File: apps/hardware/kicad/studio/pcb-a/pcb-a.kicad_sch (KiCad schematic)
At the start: 27 parts, among them J1 A PCB-K (JST-SH 10), J2 A portadora (IDC 2x15)

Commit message: feat(hardware): esquemático de la portadora de Studio y ajuste del apilado del panel
Portadora (rev 0.1, ERC sin violaciones):
- USB-C 5 V solo alimentación (CC 5.1 kΩ), polyfuse 3 A, TVS y bulk; VIN de la
  Teensy con el puente VUSB–VIN cortado.
- Teensy 4.1 como dos filas de 24 pines; USB host a USB-A; IDC 2×15 al panel con
  el mismo pinout de PCB-A; IDC 2×5 a los pines 1–10 de la Pi (5 V y UART).
- LEDs: pin 28 → 74AHCT1G125 a 5 V → puente de soldadura (saltar el buffer) → 330 Ω.
- Entrada estéreo: escalera 0/−10/−20 dB con palanca DP3T, acople, protección
  BAT54S sobre VREF de 1.65 V y seguidores MCP6004 hacia LINE IN del Audio Shield.
- Salidas 6.35 con acople, PHONES 3.5 con el sleeve en HP_VGND, CV OUT con RC de
  2 polos y seguidor.

Apilado del panel: PCB-A baja a −12.0 mm con separadores M3 estándar de 10 mm (buje
al ras, eje a 14.5 mm), PCB-K con agujeros de 8.0 mm y cuelga de los Choc, JST-SH de
entrada lateral entre placas. El pad estéreo no se lee (pin 25 libre).

Co-Authored-By: Claude Opus 5.5 <noreply@anthropic.com>
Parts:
- J1: footprint Connector_JST:JST_SH_BM10B-SRSS-TB_1x10-1MP_P1.00mm_Vertical -> Connector_JST:JST_SH_SM10B-SRSS-TB_1x10-1MP_P1.00mm_Horizontal
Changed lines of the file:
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@@
 		(date "2026-10-13")
 		(rev "0.1")
-		(comment 1 "5 ALPS EC11 (L=25, buje liso Ø6.8) + 2 RV09 B10K; placa a -11.5 mm bajo el aluminio")
+		(comment 1 "5 ALPS EC11 (L=25, buje liso Ø6.8) + 2 RV09 B10K; placa a -12.0 mm bajo el aluminio (separadores M3 de 10 mm)")
 		(comment 2 "Theory doc: apps/docs/variants/studio/theory/02-studio-pcb.md")
 	)
@@
 			)
 		)
-		(property "Footprint" "Connector_JST:JST_SH_BM10B-SRSS-TB_1x10-1MP_P1.00mm_Vertical"
+		(property "Footprint" "Connector_JST:JST_SH_SM10B-SRSS-TB_1x10-1MP_P1.00mm_Horizontal"
 			(at 229.87 149.86 0)
 			(hide yes)

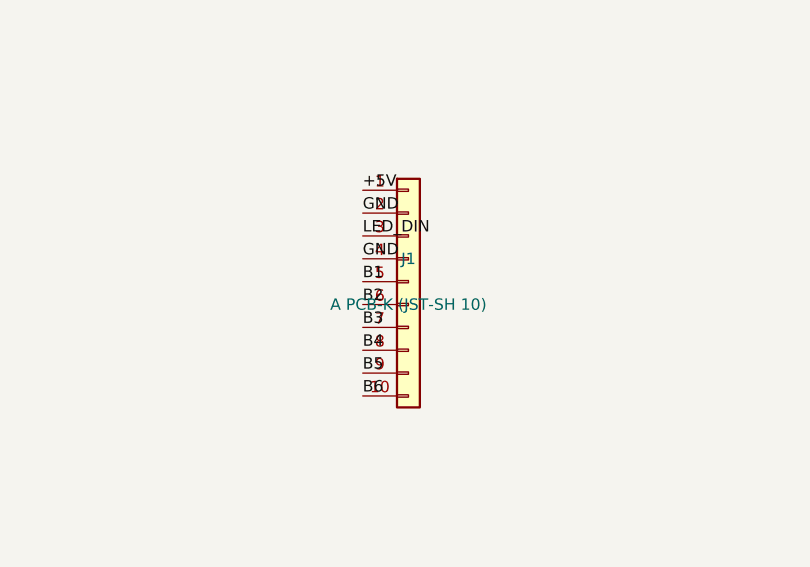
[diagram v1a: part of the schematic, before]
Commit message: feat(hardware): PCB-K ruteada (DRC limpio contra reglas de JLCPCB)
- Anillo de NAV: LEDs rotados 180° para que DOUT y DIN queden enfrentados en cada hueco (mismo
  orden e índices 0–11). Ruteo regular por script: anillo interior de +5V, saltos de datos por F.Cu
  que esquivan las ventanas de luz, una vía de GND por hueco (tools/route_pcb_k_ring.py).
- Zona de teclas con rutas explícitas (tools/route_pcb_k_keys.py): botones por F.Cu desde J1,
  cadena de datos y buses de +5V por B.Cu; capacitores de tecla a la derecha de cada LED; C19 sobre
  el bus de +5V; TP1/TP2 sobre sus pistas y fuera del BOM.
- Orden de pines de J1 nuevo en PCB-K y PCB-A (cable 1:1): B4, B6, B3, GND, +5V, GND, LED_DIN, B2,
  B5, B1. Evita ~14 cruces entre capas; los pines de la Teensy no cambian (02-studio-pcb.md §6.1).
- Planos de GND en F.Cu y B.Cu con costura cada 6 mm (tools/add_gnd_pours.py).
- Reglas de JLCPCB 2 capas en los tres proyectos: agujero-agujero 0.5 mm, vía ≥ 0.5/0.3, anillo
  ≥ 0.13; borde 0.25 mm (0.2 solo dentro de cada SK6812MINI-E).
- DRC con paridad de esquemático: 0 violaciones, 0 pads sin conectar, 0 errores de footprint.
- tools/route_board.py (Freerouting) queda como herramienta; no se usó en el resultado final.

Co-Authored-By: Claude Opus 5.5 <noreply@anthropic.com>
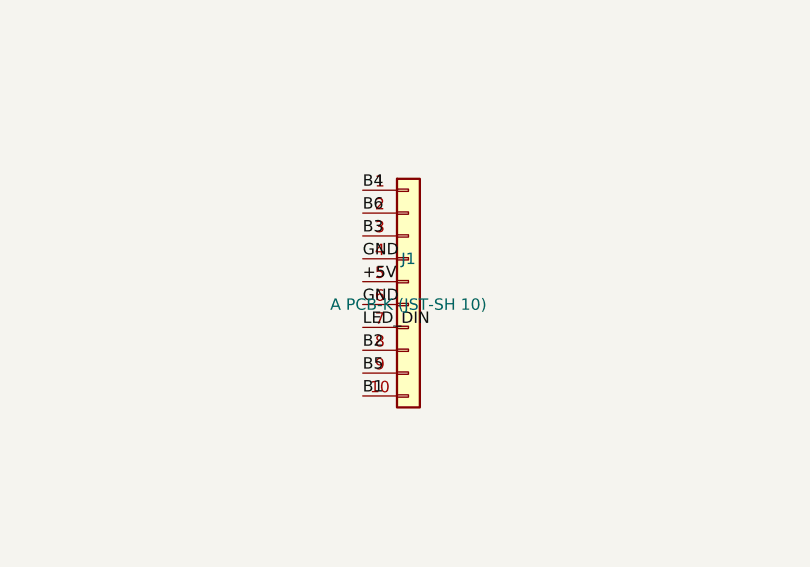
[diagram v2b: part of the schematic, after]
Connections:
- net +5V: now also J1.5 (Pin_5); no longer J1.1 (Pin_1)
- net B1: now also J1.10 (Pin_10); no longer J1.5 (Pin_5)
- net B2: now also J1.8 (Pin_8); no longer J1.6 (Pin_6)
- net B3: now also J1.3 (Pin_3); no longer J1.7 (Pin_7)
- net B4: now also J1.1 (Pin_1); no longer J1.8 (Pin_8)
- net B6: now also J1.2 (Pin_2); no longer J1.10 (Pin_10)
- net GND: now also J1.6 (Pin_6); no longer J1.2 (Pin_2)
- net LED_DIN: now also J1.7 (Pin_7); no longer J1.3 (Pin_3)
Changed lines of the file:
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@@
-	)
-	(label "+5V"
-		(at 224.79 139.70000000000002 0)
-		(effects
-			(font
-				(size 1.27 1.27)
-			)
-			(justify left bottom)
-		)
-	)
-	(label "GND"
-		(at 224.79 142.24 0)
-		(effects
-			(font
-				(size 1.27 1.27)
-			)
-			(justify left bottom)
-		)
-	)
-	(label "LED_DIN"
-		(at 224.79 144.78 0)
-		(effects
-			(font
-				(size 1.27 1.27)
-			)
-			(justify left bottom)
-		)
-	)
-	(label "GND"
-		(at 224.79 147.32000000000002 0)
-		(effects
-			(font
-				(size 1.27 1.27)
-			)
-			(justify left bottom)
-		)
-	)
-	(label "B1"
-		(at 224.79 149.86 0)
-		(effects
-			(font
-				(size 1.27 1.27)
-			)
-			(justify left bottom)
-		)
-	)
-	(label "B2"
-		(at 224.79 152.4 0)
-		(effects
-			(font
-				(size 1.27 1.27)
-			)
-			(justify left bottom)
-		)
-	)
-	(label "B3"
-		(at 224.79 154.94000000000003 0)
-		(effects
-			(font
-				(size 1.27 1.27)
-			)
-			(justify left bottom)
-		)
-	)
-	(label "B4"
-		(at 224.79 157.48000000000002 0)
-		(effects
-			(font
-				(size 1.27 1.27)
-			)
-			(justify left bottom)
-		)
-	)
-	(label "B5"
-		(at 224.79 160.02 0)
-		(effects
-			(font
-				(size 1.27 1.27)
-			)
-			(justify left bottom)
-		)
-	)
-	(label "B6"
-		(at 224.79 162.56 0)
-		(effects
-			(font
-				(size 1.27 1.27)
-			)
-			(justify left bottom)
-		)
 	)
 	(label "+5V"
@@
 			)
 			(justify left bottom)
+		)
+	)
+	(label "B4"
+		(at 224.79 139.70000000000002 0)
+		(effects
+			(font
+				(size 1.27 1.27)
+			)
+			(justify left bottom)
+		)
+	)
+	(label "B6"
+		(at 224.79 142.24 0)
+		(effects
+			(font
+				(size 1.27 1.27)
+			)
+			(justify left bottom)
+		)
+	)
+	(label "B3"
+		(at 224.79 144.78 0)
+		(effects
+			(font
+				(size 1.27 1.27)
+			)
+			(justify left bottom)
+		)
+	)
+	(label "GND"
+		(at 224.79 147.32000000000002 0)
+		(effects
+			(font
+				(size 1.27 1.27)
+			)
+			(justify left bottom)
+		)
+	)
+	(label "+5V"
+		(at 224.79 149.86 0)
+		(effects
+			(font
+				(size 1.27 1.27)
+			)
+			(justify left bottom)
+		)
+	)
+	(label "GND"
+		(at 224.79 152.4 0)
+		(effects
+			(font
+				(size 1.27 1.27)
+			)
+			(justify left bottom)
+		)
+	)
+	(label "LED_DIN"
+		(at 224.79 154.94000000000003 0)
+		(effects
+			(font
+				(size 1.27 1.27)
+			)
+			(justify left bottom)
+		)
+	)
+	(label "B2"
+		(at 224.79 157.48000000000002 0)
+		(effects
+			(font
+				(size 1.27 1.27)
+			)
+			(justify left bottom)
+		)
+	)
+	(label "B5"
+		(at 224.79 160.02 0)
+		(effects
+			(font
+				(size 1.27 1.27)
+			)
+			(justify left bottom)
+		)
+	)
+	(label "B1"
+		(at 224.79 162.56 0)
+		(effects
+			(font
+				(size 1.27 1.27)
+			)
+			(justify left bottom)

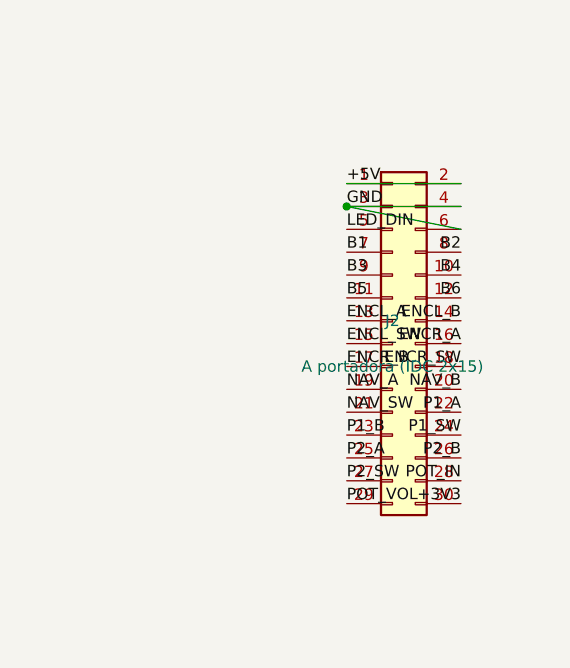
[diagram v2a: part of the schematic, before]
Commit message: feat(hardware): portadora ruteada (DRC limpio) y pinout del IDC reordenado
- Portadora: ruteo completo, DRC con paridad de esquemático 0/0/0 contra reglas de JLCPCB.
  +5V de F1 a la Pi en ~40 mm con una vía; sin paralelos audio↔digital a <1 mm.
- IDC 2×15 (PCB-A J2 ↔ portadora J5): pines ordenados por la X del pin de la Teensy al que van,
  para que el bus salga del conector sin cruces. Ambos esquemáticos re-etiquetados (ERC limpio),
  PCB-A re-ruteada (DRC 0/0/0). Tablas y razón en theory/02 §6.2.
- Herramientas: grid_route (Dijkstra en grilla 0.1 mm, 2 capas), finish_routing (rip-up and
  reroute de lo que deja Freerouting), clean_vias, add_gnd_escapes, fix_portadora_gnd,
  set_idc_pinout y build_portadora.sh (pipeline completo reproducible).

Co-Authored-By: Claude Opus 5.5 <noreply@anthropic.com>
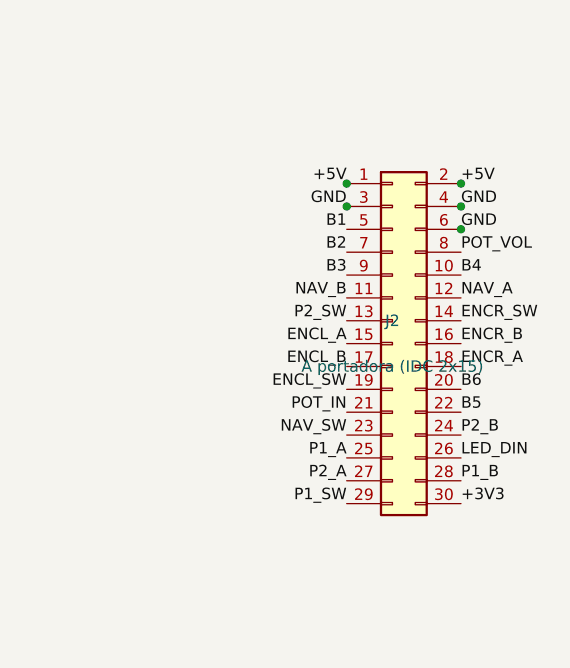
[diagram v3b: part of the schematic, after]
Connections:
- net B1: now also J2.5 (Pin_5); no longer J2.7 (Pin_7)
- net B2: now also J2.7 (Pin_7); no longer J2.8 (Pin_8)
- net B5: now also J2.22 (Pin_22); no longer J2.11 (Pin_11)
- net B6: now also J2.20 (Pin_20); no longer J2.12 (Pin_12)
- net ENCL_A: now also J2.15 (Pin_15); no longer J2.13 (Pin_13)
- net ENCL_B: now also J2.17 (Pin_17); no longer J2.14 (Pin_14)
- net ENCL_SW: now also J2.19 (Pin_19); no longer J2.15 (Pin_15)
- net ENCR_A: now also J2.18 (Pin_18); no longer J2.16 (Pin_16)
- net ENCR_B: now also J2.16 (Pin_16); no longer J2.17 (Pin_17)
- net ENCR_SW: now also J2.14 (Pin_14); no longer J2.18 (Pin_18)
- net LED_DIN: now also J2.26 (Pin_26); no longer J2.5 (Pin_5)
- net NAV_A: now also J2.12 (Pin_12); no longer J2.19 (Pin_19)
- net NAV_B: now also J2.11 (Pin_11); no longer J2.20 (Pin_20)
- net NAV_SW: now also J2.23 (Pin_23); no longer J2.21 (Pin_21)
- net P1_A: now also J2.25 (Pin_25); no longer J2.22 (Pin_22)
- net P1_B: now also J2.28 (Pin_28); no longer J2.23 (Pin_23)
- net P1_SW: now also J2.29 (Pin_29); no longer J2.24 (Pin_24)
- net P2_A: now also J2.27 (Pin_27); no longer J2.25 (Pin_25)
- net P2_B: now also J2.24 (Pin_24); no longer J2.26 (Pin_26)
- net P2_SW: now also J2.13 (Pin_13); no longer J2.27 (Pin_27)
- net POT_IN: now also J2.21 (Pin_21); no longer J2.28 (Pin_28)
- net POT_VOL: now also J2.8 (Pin_8); no longer J2.29 (Pin_29)

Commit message: feat(hardware): archivos de fabricación JLCPCB y shield corregido en la portadora
- Portadora: las filas del Audio Shield estaban al revés (quedaba espejado respecto de la Teensy con el
  shield boca arriba). J16 (GND/0–12) pasa atrás y J15 adelante; re-ruteada, DRC con paridad 0/0/0.
- Números LCSC en los tres esquemáticos (set_lcsc.py), todo en ensamble Economic. PCB-K pasa al
  SK6812MINI-EA (mismo pinout y cuerpo, sin la restricción Standard-only del MINI-E).
- Escalera del PAD y acople al codec con valores Basic (33k/12k/5.1k, 4.7 µF): la simulación sigue
  pasando C1–C6 (tercera corrida en theory/03).
- export_fab.py: Gerbers + taladros, BOM y CPL en formato JLC; los THT usan el centro de sus pads y los
  IDC la rotación del modelo de JLC. Portadora con jacks e IDC ensamblados; el resto de los THT en
  fab/lcsc-piezas-sueltas.csv.
- sync_fp_fields.py también copia Value y LCSC a las placas.
- theory/02 §10C–10D: fabricación, montaje del shield, J9, J3 (USB host), corriente de la Pi y la
  verificación de punta a punta de las conexiones.

Co-Authored-By: Claude Opus 5.5 <noreply@anthropic.com>
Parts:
- C1, C10, C11, C12, C13, C14, C15, C2, C3, C4, C5, C6, C7, C8, C9: LCSC (none) -> C57112
- C16, C17: LCSC (none) -> C14663
- C18: LCSC (none) -> C15850
- J1: LCSC (none) -> C160409
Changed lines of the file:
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@@
+			)
+		)
+		(property "LCSC" "C57112"
+			(at 44.45 85.09 0)
+			(hide yes)
+			(show_name no)
+			(do_not_autoplace no)
+			(effects
+				(font
+					(size 1.27 1.27)
+				)
 			)
 		)
@@
 			)
 		)
+		(property "LCSC" "C57112"
+			(at 59.69 85.09 0)
+			(hide yes)
+			(show_name no)
+			(do_not_autoplace no)
+			(effects
+				(font
+					(size 1.27 1.27)
+				)
+			)
+		)
 		(property "Description" "Unpolarized capacitor"
 			(at 59.69 85.09 0)
@@
 			)
 		)
+		(property "LCSC" "C57112"
+			(at 74.93 85.09 0)
+			(hide yes)
+			(show_name no)
+			(do_not_autoplace no)
+			(effects
+				(font
+					(size 1.27 1.27)
+				)
+			)
+		)
 		(property "Description" "Unpolarized capacitor"
 			(at 74.93 85.09 0)
@@
 			)
 		)
+		(property "LCSC" "C57112"
+			(at 105.41 85.09 0)
+			(hide yes)
+			(show_name no)
+			(do_not_autoplace no)
+			(effects
+				(font
+					(size 1.27 1.27)
+				)
+			)
+		)
 		(property "Description" "Unpolarized capacitor"
 			(at 105.41 85.09 0)
@@
 			)
 		)
+		(property "LCSC" "C57112"
+			(at 119.38 85.09 0)
+			(hide yes)
+			(show_name no)
+			(do_not_autoplace no)
+			(effects
+				(font
+					(size 1.27 1.27)
+				)
+			)
+		)
 		(property "Description" "Unpolarized capacitor"
 			(at 119.38 85.09 0)
@@
 			)
 		)
+		(property "LCSC" "C57112"
+			(at 134.62 85.09 0)
+			(hide yes)
+			(show_name no)
+			(do_not_autoplace no)
+			(effects
+				(font
+					(size 1.27 1.27)
+				)
+			)
+		)
 		(property "Description" "Unpolarized capacitor"
 			(at 134.62 85.09 0)
@@
 			)
 		)
+		(property "LCSC" "C57112"
+			(at 165.1 85.09 0)
+			(hide yes)
+			(show_name no)
+			(do_not_autoplace no)
+			(effects
+				(font
+					(size 1.27 1.27)
+				)
+			)
+		)
 		(property "Description" "Unpolarized capacitor"
 			(at 165.1 85.09 0)
@@
 			)
 		)
+		(property "LCSC" "C57112"
+			(at 180.34 85.09 0)
+			(hide yes)
+			(show_name no)
+			(do_not_autoplace no)
+			(effects
+				(font
+					(size 1.27 1.27)
+				)
+			)
+		)
 		(property "Description" "Unpolarized capacitor"
 			(at 180.34 85.09 0)
@@
 			)
 		)
+		(property "LCSC" "C57112"
+			(at 195.58 85.09 0)
+			(hide yes)
+			(show_name no)
+			(do_not_autoplace no)
+			(effects
+				(font
+					(size 1.27 1.27)
+				)
+			)
+		)
 		(property "Description" "Unpolarized capacitor"
 			(at 195.58 85.09 0)
@@
 			)
 		)
+		(property "LCSC" "C57112"
+			(at 224.79 85.09 0)
+			(hide yes)
+			(show_name no)
+			(do_not_autoplace no)
+			(effects
+				(font
+					(size 1.27 1.27)
+				)
+			)
+		)
 		(property "Description" "Unpolarized capacitor"
 			(at 224.79 85.09 0)
@@
 			)
 		)
+		(property "LCSC" "C57112"
+			(at 240.03 85.09 0)
+			(hide yes)
+			(show_name no)
+			(do_not_autoplace no)
+			(effects
+				(font
+					(size 1.27 1.27)
+				)
+			)
+		)
 		(property "Description" "Unpolarized capacitor"
 			(at 240.03 85.09 0)
@@
 			)
 		)
+		(property "LCSC" "C57112"
+			(at 255.27 85.09 0)
+			(hide yes)
+			(show_name no)
+			(do_not_autoplace no)
+			(effects
+				(font
+					(size 1.27 1.27)
+				)
+			)
+		)
 		(property "Description" "Unpolarized capacitor"
 			(at 255.27 85.09 0)
@@
 			)
 		)
+		(property "LCSC" "C57112"
+			(at 284.48 85.09 0)
+			(hide yes)
+			(show_name no)
+			(do_not_autoplace no)
+			(effects
+				(font
+					(size 1.27 1.27)
+				)
+			)
+		)
 		(property "Description" "Unpolarized capacitor"
 			(at 284.48 85.09 0)
@@
 			)
 		)
+		(property "LCSC" "C57112"
+			(at 299.72 85.09 0)
+			(hide yes)
+			(show_name no)
+			(do_not_autoplace no)
+			(effects
+				(font
+					(size 1.27 1.27)
+				)
+			)
+		)
 		(property "Description" "Unpolarized capacitor"
 			(at 299.72 85.09 0)
@@
 			)
 		)
+		(property "LCSC" "C57112"
+			(at 314.96 85.09 0)
+			(hide yes)
+			(show_name no)
+			(do_not_autoplace no)
+			(effects
+				(font
+					(size 1.27 1.27)
+				)
+			)
+		)
 		(property "Description" "Unpolarized capacitor"
 			(at 314.96 85.09 0)
@@
 			)
 		)
+		(property "LCSC" "C14663"
+			(at 100.33 149.86 0)
+			(hide yes)
+			(show_name no)
+			(do_not_autoplace no)
+			(effects
+				(font
+					(size 1.27 1.27)
+				)
+			)
+		)
 		(property "Description" "Unpolarized capacitor"
 			(at 100.33 149.86 0)
@@
 			)
 		)
+		(property "LCSC" "C14663"
+			(at 149.86 149.86 0)
+			(hide yes)
+			(show_name no)
+			(do_not_autoplace no)
+			(effects
+				(font
+					(size 1.27 1.27)
+				)
+			)
+		)
 		(property "Description" "Unpolarized capacitor"
 			(at 149.86 149.86 0)
@@
 			)
 		)
+		(property "LCSC" "C15850"
+			(at 175.26 149.86 0)
+			(hide yes)
+			(show_name no)
+			(do_not_autoplace no)
+			(effects
+				(font
+					(size 1.27 1.27)
+				)
+			)
+		)
 		(property "Description" "Unpolarized capacitor"
 			(at 175.26 149.86 0)
@@
 			(at 229.87 149.86 0)
 			(hide yes)
+			(show_name no)
+			(do_not_autoplace no)
+			(effects
+				(font
+					(size 1.27 1.27)
+				)
+			)
+		)
+		(property "LCSC" "C160409"
+			(at 229.87 149.86 0)
+			(hide yes)

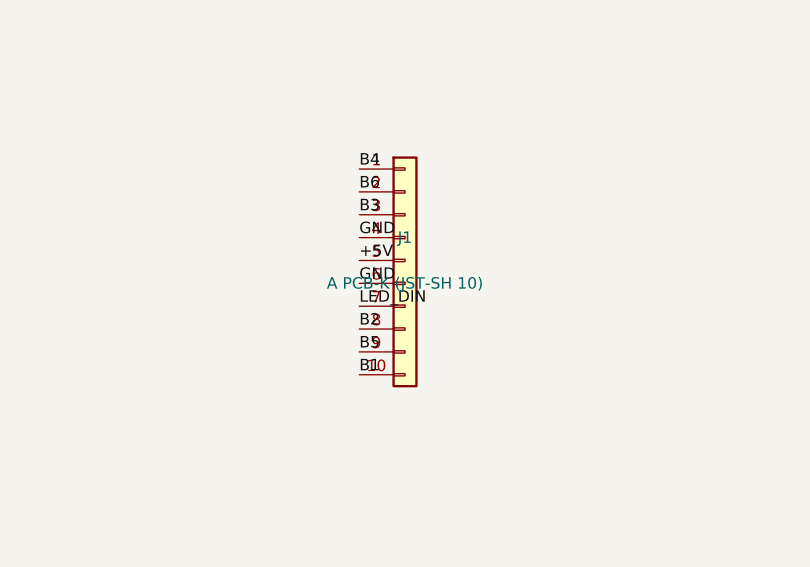
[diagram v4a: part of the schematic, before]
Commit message: feat(studio): prototipo económico de 2 placas, enclosure validado en FreeCAD y conectores de chasis
Placas (ADR-004 rev. 3, theory/02 §10F):
- Sin PCB-K ni LEDs montados: los Choc se cablean a J1 de PCB-A, que pasa de JST-SH a header 1×10 acodado
  con el mismo pinout (+5V y LED_DIN libres). PCB-A re-ruteada (build_pcb_a.sh), DRC con paridad 0/0/0.
- Portadora con ensamble solo de SMD; PCB-A solo PCB. export_fab.py genera solo esas dos.
- Todos los conectores traseros de chasis, cableados a los pads de los footprints de jacks (§10H).

Enclosure (apps/design/3d-models/studio, theory/02 §10E–10H):
- Modelo FreeCAD con las placas de KiCad: caja 48/83 a 12°, portadora corrida +16 mm en X para librar el
  GPIO de la Pi con el shield sobre headers.
- Pantalla sujeta con dos barras de PETG a 4 espárragos PEM; aluminio fijado con 6 M3 avellanados.
- Pared trasera en una sola fila (z 22), HOST en USB-A; separadores de la portadora y patas.
- Anillo WS2812 de NAV bajo un difusor Ø44 y soportes impresos para APA102 bajo cada Choc.
- Archivos: cuerpo-petg.stl, barras, soportes de tecla, panel-aluminio.dxf (3 capas), difusor-nav.dxf.

Co-Authored-By: Claude Opus 5.5 <noreply@anthropic.com>
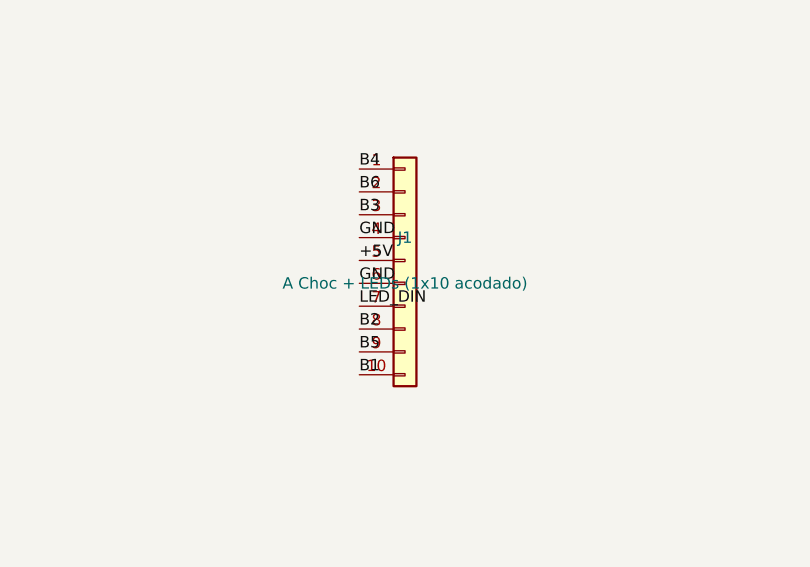
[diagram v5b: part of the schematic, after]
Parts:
- J1: value A PCB-K (JST-SH 10) -> A Choc + LEDs (1x10 acodado); footprint Connector_JST:JST_SH_SM10B-SRSS-TB_1x10-1MP_P1.00mm_Horizontal -> Connector_PinHeader_2.54mm:PinHeader_1x10_P2.54mm_Horizontal; LCSC C160409 -> (none)
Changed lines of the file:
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@@
 			)
 		)
-		(property "Value" "A PCB-K (JST-SH 10)"
+		(property "Value" "A Choc + LEDs (1x10 acodado)"
 			(at 229.87 152.4 0)
 			(show_name no)
@@
 			)
 		)
-		(property "Footprint" "Connector_JST:JST_SH_SM10B-SRSS-TB_1x10-1MP_P1.00mm_Horizontal"
+		(property "Footprint" "Connector_PinHeader_2.54mm:PinHeader_1x10_P2.54mm_Horizontal"
 			(at 229.87 149.86 0)
 			(hide yes)
@@
 			(at 229.87 149.86 0)
 			(hide yes)
-			(show_name no)
-			(do_not_autoplace no)
-			(effects
-				(font
-					(size 1.27 1.27)
-				)
-			)
-		)
-		(property "LCSC" "C160409"
-			(at 229.87 149.86 0)
-			(hide yes)
